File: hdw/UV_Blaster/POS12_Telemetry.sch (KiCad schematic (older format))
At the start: 7 parts

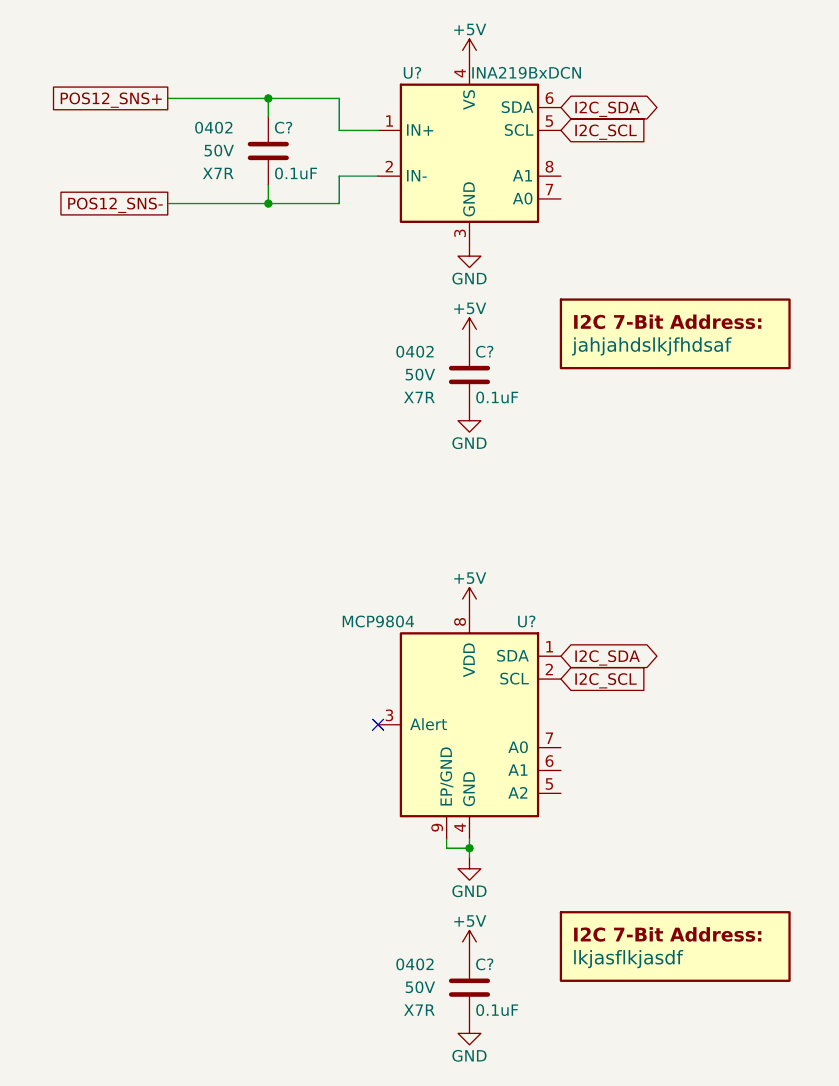
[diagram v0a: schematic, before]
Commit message: More sch work, netlist, part numbers, footprints
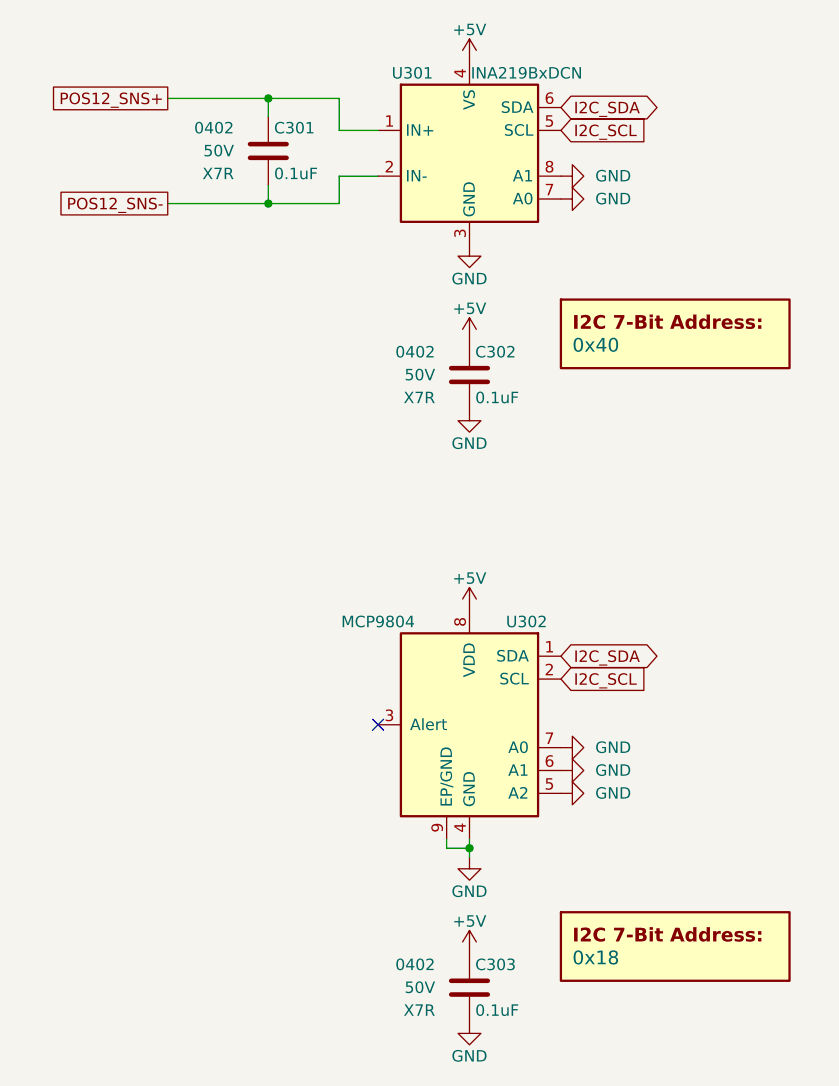
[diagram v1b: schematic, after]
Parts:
- C301, C302, C303: renamed from C?; Configuration (none) -> Telemetry
- DOC301: renamed from DOC?; value jahjahdslkjfhdsaf -> 0x40
- DOC302: renamed from DOC?; value lkjasflkjasdf -> 0x18
- U301, U302: renamed from U?; Configuration (none) -> Telemetry
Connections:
- net GND: now also U301.7 (A0), U301.8 (A1), U302.5 (A2), U302.6 (A1), U302.7 (A0)
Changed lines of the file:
@@
 encoding utf-8
 Sheet 3 14
-Title ""
-Date ""
-Rev ""
-Comp ""
+Title "UV Blaster"
+Date "2020-05-07"
+Rev "A"
+Comp "Drew Maatman"
 Comment1 ""
 Comment2 ""
@@
 AR Path="/5E052856/5E0ACFF2" Ref="#PWR?"  Part="1"
 AR Path="/5E939D24/5E0ACFF2" Ref="#PWR?"  Part="1"
-AR Path="/5E9E0E9F/5E0ACFF2" Ref="#PWR?"  Part="1"
-F 0 "#PWR?" H 5110 2190 50  0001 C CNN
+AR Path="/5E9E0E9F/5E0ACFF2" Ref="#PWR0302"  Part="1"
+F 0 "#PWR0302" H 5110 2190 50  0001 C CNN
 F 1 "GND" H 5110 2290 50  0000 C CNN
 F 2 "" H 5110 2440 50  0001 C CNN
@@
 AR Path="/5E052856/5E0B2427" Ref="C?"  Part="1"
 AR Path="/5E939D24/5E0B2427" Ref="C?"  Part="1"
-AR Path="/5E9E0E9F/5E0B2427" Ref="C?"  Part="1"
-F 0 "C?" H 5135 3110 50  0000 L CNN
+AR Path="/5E9E0E9F/5E0B2427" Ref="C302"  Part="1"
+F 0 "C302" H 5135 3110 50  0000 L CNN
 F 1 "0.1uF" H 5135 2910 50  0000 L CNN
 F 2 "Capacitors_SMD:C_0402" H 5148 2860 50  0001 C CNN
@@
 F 6 "X7R" H 4960 2910 50  0000 R CNN "Dielectric"
 F 7 "490-10701-1-ND" H 1200 -3870 50  0001 C CNN "Digi-Key PN"
+F 8 "Telemetry" H 5110 3010 50  0001 C CNN "Configuration"
 	1    5110 3010
 	1    0    0    -1
@@
 AR Path="/5E052856/5E0B592B" Ref="#PWR?"  Part="1"
 AR Path="/5E939D24/5E0B592B" Ref="#PWR?"  Part="1"
-AR Path="/5E9E0E9F/5E0B592B" Ref="#PWR?"  Part="1"
-F 0 "#PWR?" H 5110 2910 50  0001 C CNN
+AR Path="/5E9E0E9F/5E0B592B" Ref="#PWR0304"  Part="1"
+F 0 "#PWR0304" H 5110 2910 50  0001 C CNN
 F 1 "GND" H 5110 3010 50  0000 C CNN
 F 2 "" H 5110 3160 50  0001 C CNN
@@
 AR Path="/5E052856/5E2AA995" Ref="#PWR?"  Part="1"
 AR Path="/5E939D24/5E2AA995" Ref="#PWR?"  Part="1"
-AR Path="/5E9E0E9F/5E2AA995" Ref="#PWR?"  Part="1"
-F 0 "#PWR?" H 5110 4870 50  0001 C CNN
+AR Path="/5E9E0E9F/5E2AA995" Ref="#PWR0306"  Part="1"
+F 0 "#PWR0306" H 5110 4870 50  0001 C CNN
 F 1 "GND" H 5110 4970 50  0000 C CNN
 F 2 "" H 5110 5120 50  0001 C CNN
@@
 AR Path="/5E052856/5E2AA99D" Ref="U?"  Part="1"
 AR Path="/5E939D24/5E2AA99D" Ref="U?"  Part="1"
-AR Path="/5E9E0E9F/5E2AA99D" Ref="U?"  Part="1"
-F 0 "U?" H 4860 4990 50  0000 C CNN
+AR Path="/5E9E0E9F/5E2AA99D" Ref="U302"  Part="1"
+F 0 "U302" H 4860 4990 50  0000 C CNN
 F 1 "MCP9804" H 5510 4990 50  0000 C CNN
 F 2 "Package_DFN_QFN:DFN-8-1EP_3x2mm_P0.5mm_EP1.3x1.5mm" H 4010 4040 50  0001 C CNN
 F 3 "http://ww1.microchip.com/downloads/en/DeviceDoc/22203b.pdf" H 4860 4990 50  0001 C CNN
 F 4 "MCP9804T-E/MCCT-ND" H 5110 4540 50  0001 C CNN "Digi-Key PN"
+F 5 "Telemetry" H 5110 4540 50  0001 C CNN "Configuration"
 	1    5110 4540
 	-1   0    0    -1
@@
 AR Path="/5E052856/5E2AA9A1" Ref="C?"  Part="1"
 AR Path="/5E939D24/5E2AA9A1" Ref="C?"  Part="1"
-AR Path="/5E9E0E9F/5E2AA9A1" Ref="C?"  Part="1"
-F 0 "C?" H 5135 5790 50  0000 L CNN
+AR Path="/5E9E0E9F/5E2AA9A1" Ref="C303"  Part="1"
+F 0 "C303" H 5135 5790 50  0000 L CNN
 F 1 "0.1uF" H 5135 5590 50  0000 L CNN
 F 2 "Capacitors_SMD:C_0402" H 5148 5540 50  0001 C CNN
@@
 F 6 "X7R" H 4960 5590 50  0000 R CNN "Dielectric"
 F 7 "490-10701-1-ND" H 1200 -1190 50  0001 C CNN "Digi-Key PN"
+F 8 "Telemetry" H 5110 5690 50  0001 C CNN "Configuration"
 	1    5110 5690
 	1    0    0    -1
@@
 AR Path="/5E052856/5E2AA9AD" Ref="#PWR?"  Part="1"
 AR Path="/5E939D24/5E2AA9AD" Ref="#PWR?"  Part="1"
-AR Path="/5E9E0E9F/5E2AA9AD" Ref="#PWR?"  Part="1"
-F 0 "#PWR?" H 5110 5590 50  0001 C CNN
+AR Path="/5E9E0E9F/5E2AA9AD" Ref="#PWR0308"  Part="1"
+F 0 "#PWR0308" H 5110 5590 50  0001 C CNN
 F 1 "GND" H 5110 5690 50  0000 C CNN
 F 2 "" H 5110 5840 50  0001 C CNN
@@
 AR Path="/5E052856/5E07E0FD" Ref="C?"  Part="1"
 AR Path="/5E939D24/5E07E0FD" Ref="C?"  Part="1"
-AR Path="/5E9E0E9F/5E07E0FD" Ref="C?"  Part="1"
-F 0 "C?" H 4255 2130 50  0000 L CNN
+AR Path="/5E9E0E9F/5E07E0FD" Ref="C301"  Part="1"
+F 0 "C301" H 4255 2130 50  0000 L CNN
 F 1 "0.1uF" H 4255 1930 50  0000 L CNN
 F 2 "Capacitors_SMD:C_0402" H 4268 1880 50  0001 C CNN
@@
 F 6 "X7R" H 4080 1930 50  0000 R CNN "Dielectric"
 F 7 "490-10701-1-ND" H 320 -4850 50  0001 C CNN "Digi-Key PN"
+F 8 "Telemetry" H 4230 2030 50  0001 C CNN "Configuration"
 	1    4230 2030
 	1    0    0    -1
@@
 	3790 1800 4230 1800
 $Comp
-L Analog_ADC:INA219BxDCN U?
+L Analog_ADC:INA219BxDCN U301
 U 1 1 5E1AAC3C
 P 5110 2040
-F 0 "U?" H 4860 2390 50  0000 C CNN
+F 0 "U301" H 4860 2390 50  0000 C CNN
 F 1 "INA219BxDCN" H 5360 2390 50  0000 C CNN
 F 2 "Package_TO_SOT_SMD:SOT-23-8" H 5760 1690 50  0001 C CNN
 F 3 "http://www.ti.com/lit/ds/symlink/ina219.pdf" H 5460 1940 50  0001 C CNN
 F 4 "296-46420-1-ND" H 5110 2040 50  0001 C CNN "Digi-Key PN"
+F 5 "Telemetry" H 5110 2040 50  0001 C CNN "Configuration"
 	1    5110 2040
 	1    0    0    -1
@@
 AR Path="/5E052856/5E0B8BC8" Ref="DOC?"  Part="1"
 AR Path="/5E939D24/5E0B8BC8" Ref="DOC?"  Part="1"
-AR Path="/5E9E0E9F/5E0B8BC8" Ref="DOC?"  Part="1"
-F 0 "DOC?" H 6010 3130 60  0001 C CNN
-F 1 "jahjahdslkjfhdsaf" H 5560 2880 60  0000 L CNN
+AR Path="/5E9E0E9F/5E0B8BC8" Ref="DOC301"  Part="1"
+F 0 "DOC301" H 6010 3130 60  0001 C CNN
+F 1 "0x40" H 5560 2880 60  0000 L CNN
 F 2 "" H 6010 3230 60  0001 C CNN
 F 3 "" H 6010 3230 60  0001 C CNN
@@
 AR Path="/5E052856/5E2AA9AF" Ref="DOC?"  Part="1"
 AR Path="/5E939D24/5E2AA9AF" Ref="DOC?"  Part="1"
-AR Path="/5E9E0E9F/5E2AA9AF" Ref="DOC?"  Part="1"
-F 0 "DOC?" H 6010 5810 60  0001 C CNN
-F 1 "lkjasflkjasdf" H 5560 5560 60  0000 L CNN
+AR Path="/5E9E0E9F/5E2AA9AF" Ref="DOC302"  Part="1"
+F 0 "DOC302" H 6010 5810 60  0001 C CNN
+F 1 "0x18" H 5560 5560 60  0000 L CNN
 F 2 "" H 6010 5910 60  0001 C CNN
 F 3 "" H 6010 5910 60  0001 C CNN
@@
 $EndComp
 $Comp
-L power:+5V #PWR?
+L power:+5V #PWR0301
 U 1 1 5EA86A51
 P 5110 1640
-F 0 "#PWR?" H 5110 1490 50  0001 C CNN
+F 0 "#PWR0301" H 5110 1490 50  0001 C CNN
 F 1 "+5V" H 5110 1780 50  0000 C CNN
 F 2 "" H 5110 1640 50  0001 C CNN
@@
 $EndComp
 $Comp
-L power:+5V #PWR?
+L power:+5V #PWR0305
 U 1 1 5EA87055
 P 5110 4040
-F 0 "#PWR?" H 5110 3890 50  0001 C CNN
+F 0 "#PWR0305" H 5110 3890 50  0001 C CNN
 F 1 "+5V" H 5110 4180 50  0000 C CNN
 F 2 "" H 5110 4040 50  0001 C CNN
@@
 $EndComp
 $Comp
-L power:+5V #PWR?
+L power:+5V #PWR0303
 U 1 1 5EA883CC
 P 5110 2860
-F 0 "#PWR?" H 5110 2710 50  0001 C CNN
+F 0 "#PWR0303" H 5110 2710 50  0001 C CNN
 F 1 "+5V" H 5110 3000 50  0000 C CNN
 F 2 "" H 5110 2860 50  0001 C CNN
@@
 $EndComp
 $Comp
-L power:+5V #PWR?
+L power:+5V #PWR0307
 U 1 1 5EA88B50
 P 5110 5540
-F 0 "#PWR?" H 5110 5390 50  0001 C CNN
+F 0 "#PWR0307" H 5110 5390 50  0001 C CNN
 F 1 "+5V" H 5110 5680 50  0000 C CNN
 F 2 "" H 5110 5540 50  0001 C CNN
@@
 	1    0    0    -1
 $EndComp
+$Comp
+L power:GND #PWR0310
+U 1 1 5EBFD651
+P 5510 2240
+F 0 "#PWR0310" H 5510 1990 50  0001 C CNN
+F 1 "GND" V 5510 2090 50  0000 R CNN
+F 2 "" H 5510 2240 50  0001 C CNN
+F 3 "" H 5510 2240 50  0001 C CNN
+	1    5510 2240
+	0    -1   -1   0
+$EndComp
+$Comp
+L power:GND #PWR0309
+U 1 1 5EBFDA00
+P 5510 2140
+F 0 "#PWR0309" H 5510 1890 50  0001 C CNN
+F 1 "GND" V 5510 1990 50  0000 R CNN
+F 2 "" H 5510 2140 50  0001 C CNN
+F 3 "" H 5510 2140 50  0001 C CNN
+	1    5510 2140
+	0    -1   -1   0
+$EndComp
+$Comp
+L power:GND #PWR0313
+U 1 1 5EC10787
+P 5510 4840
+F 0 "#PWR0313" H 5510 4590 50  0001 C CNN
+F 1 "GND" V 5510 4690 50  0000 R CNN
+F 2 "" H 5510 4840 50  0001 C CNN
+F 3 "" H 5510 4840 50  0001 C CNN
+	1    5510 4840
+	0    -1   -1   0
+$EndComp
+$Comp
+L power:GND #PWR0312
+U 1 1 5EC10EC4
+P 5510 4740
+F 0 "#PWR0312" H 5510 4490 50  0001 C CNN
+F 1 "GND" V 5510 4590 50  0000 R CNN
+F 2 "" H 5510 4740 50  0001 C CNN
+F 3 "" H 5510 4740 50  0001 C CNN
+	1    5510 4740
+	0    -1   -1   0
+$EndComp
+$Comp
+L power:GND #PWR0311
+U 1 1 5EC1125A
+P 5510 4640
+F 0 "#PWR0311" H 5510 4390 50  0001 C CNN
+F 1 "GND" V 5510 4490 50  0000 R CNN
+F 2 "" H 5510 4640 50  0001 C CNN
+F 3 "" H 5510 4640 50  0001 C CNN
+	1    5510 4640
+	0    -1   -1   0
+$EndComp
 $EndSCHEMATC
